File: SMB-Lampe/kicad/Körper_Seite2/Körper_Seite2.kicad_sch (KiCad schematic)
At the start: 0 parts

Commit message: Alle Platinen erstellt
Alle Platinen wurden im Projekt einzeln erstellt.
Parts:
- added C12, C13, C14, C15, C16, C17, C18, C19, C20: 100nF, Capacitor_SMD:C_0201_0603Metric, symbol Device:C
- added D12, D13, D14, D15, D16, D17, D18, D19, D20: WS2812B, LED_SMD:LED_WS2812B_PLCC4_5.0x5.0mm_P3.2mm, symbol LED:WS2812B
- added J13, J14, J15, J16, J17, J18: Conn_01x01_Pin, TestPoint:TestPoint_Pad_1.0x1.0mm, symbol Connector:Conn_01x01_Pin
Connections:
- new net: D13.4 (DIN), D14.2 (DOUT)
- new net: D14.4 (DIN), D15.2 (DOUT)
- new net: D17.4 (DIN), D18.2 (DOUT)
- new net: D18.4 (DIN), D19.2 (DOUT)
- new net: D19.4 (DIN), D20.2 (DOUT)
- new net: D15.4 (DIN), D16.2 (DOUT)
- new net: D12.4 (DIN), D13.2 (DOUT)
- new net Data: D16.4 (DIN), D17.2 (DOUT)
- new net Data_In: D12.2 (DOUT), J14.1 (Pin_1)
- new net Data_OUT: D20.4 (DIN), J17.1 (Pin_1)
- new net GND: C12.1, C12.2, C13.1, C13.2, C14.1, C14.2, C15.1, C15.2, C16.1, C16.2, C17.1, C17.2, C18.1, C18.2, C19.1, C19.2, C20.1, C20.2, D12.1 (VDD), D12.3 (VSS), D13.1 (VDD), D13.3 (VSS), D14.1 (VDD), D14.3 (VSS), D15.1 (VDD), D15.3 (VSS), D16.1 (VDD), D16.3 (VSS), D17.1 (VDD), D17.3 (VSS), D18.1 (VDD), D18.3 (VSS), D19.1 (VDD), D19.3 (VSS), D20.1 (VDD), D20.3 (VSS), J13.1 (Pin_1), J15.1 (Pin_1), J16.1 (Pin_1), J18.1 (Pin_1)

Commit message: Alle LEDs nochmal richtig angeschlossen
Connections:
- net Data: now also D16.2 (DOUT), D17.4 (DIN); no longer D16.4 (DIN), D17.2 (DOUT)
- net Data_In: now also D12.4 (DIN); no longer D12.2 (DOUT)
- net Data_OUT: now also D20.2 (DOUT); no longer D20.4 (DIN)
- net GND: no longer C12.1, C13.1, C14.1, C15.1, C16.1, C17.1, C18.1, C19.1, C20.1, D12.1 (VDD), D13.1 (VDD), D14.1 (VDD), D15.1 (VDD), D16.1 (VDD), D17.1 (VDD), D18.1 (VDD), D19.1 (VDD), D20.1 (VDD), J13.1 (Pin_1), J16.1 (Pin_1)
- net at D14.2 (DOUT): now also D15.4 (DIN); no longer D13.4 (DIN)
- net at D14.4 (DIN): now also D13.2 (DOUT); no longer D15.2 (DOUT)
- net at D18.2 (DOUT): now also D19.4 (DIN); no longer D17.4 (DIN)
- net at D18.4 (DIN): now also D17.2 (DOUT); no longer D19.2 (DOUT)
- new net: D19.2 (DOUT), D20.4 (DIN)
- new net: D15.2 (DOUT), D16.4 (DIN)
- new net: D12.2 (DOUT), D13.4 (DIN)
- new net +5V: C12.1, C13.1, C14.1, C15.1, C16.1, C17.1, C18.1, C19.1, C20.1, D12.1 (VDD), D13.1 (VDD), D14.1 (VDD), D15.1 (VDD), D16.1 (VDD), D17.1 (VDD), D18.1 (VDD), D19.1 (VDD), D20.1 (VDD), J13.1 (Pin_1), J16.1 (Pin_1)
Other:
- moved on the sheet: C12, C13, C14, C15, C16, C17, C18, C19, C20

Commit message: Hinterbein Seite 1/2 erstellt
Anschlüsse zwischen den Platinen mit MountingHoles. Eigenes MountingHole Erstellt
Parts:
- J13, J14, J15, J16, J17, J18: footprint TestPoint:TestPoint_Pad_1.0x1.0mm -> TestPoint:TestPoint_Pad_2.0x2.0mm
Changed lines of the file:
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@@
 			)
 		)
-		(property "Footprint" "TestPoint:TestPoint_Pad_1.0x1.0mm"
+		(property "Footprint" "TestPoint:TestPoint_Pad_2.0x2.0mm"
 			(at 259.08 120.65 0)
 			(effects
@@
 			)
 		)
-		(property "Footprint" "TestPoint:TestPoint_Pad_1.0x1.0mm"
+		(property "Footprint" "TestPoint:TestPoint_Pad_2.0x2.0mm"
 			(at 33.02 63.5 0)
 			(effects
@@
 			)
 		)
-		(property "Footprint" "TestPoint:TestPoint_Pad_1.0x1.0mm"
+		(property "Footprint" "TestPoint:TestPoint_Pad_2.0x2.0mm"
 			(at 33.02 25.4 0)
 			(effects
@@
 			)
 		)
-		(property "Footprint" "TestPoint:TestPoint_Pad_1.0x1.0mm"
+		(property "Footprint" "TestPoint:TestPoint_Pad_2.0x2.0mm"
 			(at 33.02 44.45 0)
 			(effects
@@
 			)
 		)
-		(property "Footprint" "TestPoint:TestPoint_Pad_1.0x1.0mm"
+		(property "Footprint" "TestPoint:TestPoint_Pad_2.0x2.0mm"
 			(at 259.08 101.6 0)
 			(effects
@@
 			)
 		)
-		(property "Footprint" "TestPoint:TestPoint_Pad_1.0x1.0mm"
+		(property "Footprint" "TestPoint:TestPoint_Pad_2.0x2.0mm"
 			(at 259.08 139.7 0)
 			(effects

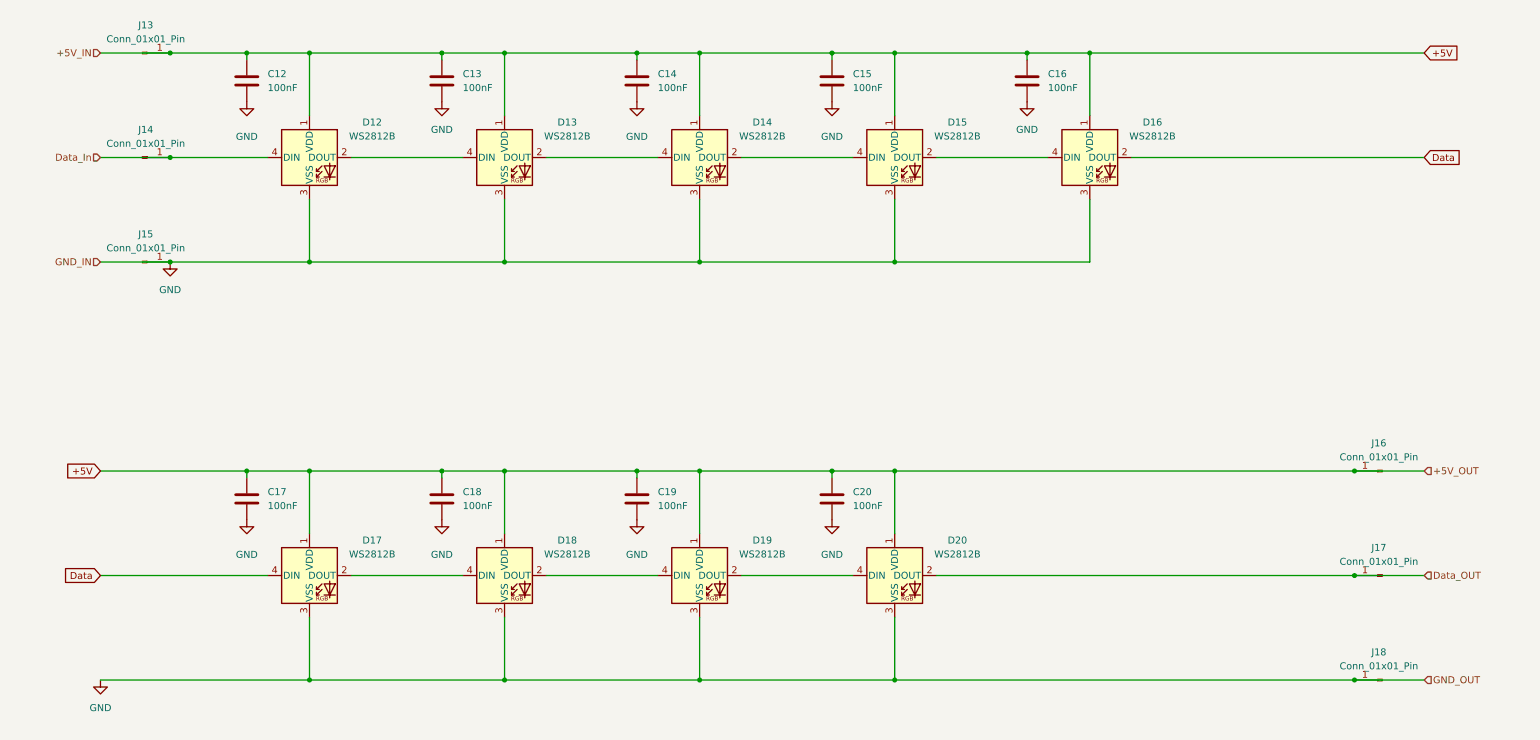
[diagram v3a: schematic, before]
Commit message: Vorderseite Platine Körper Seite 1 fertig
zwei GND Verbindungen fehlen noch
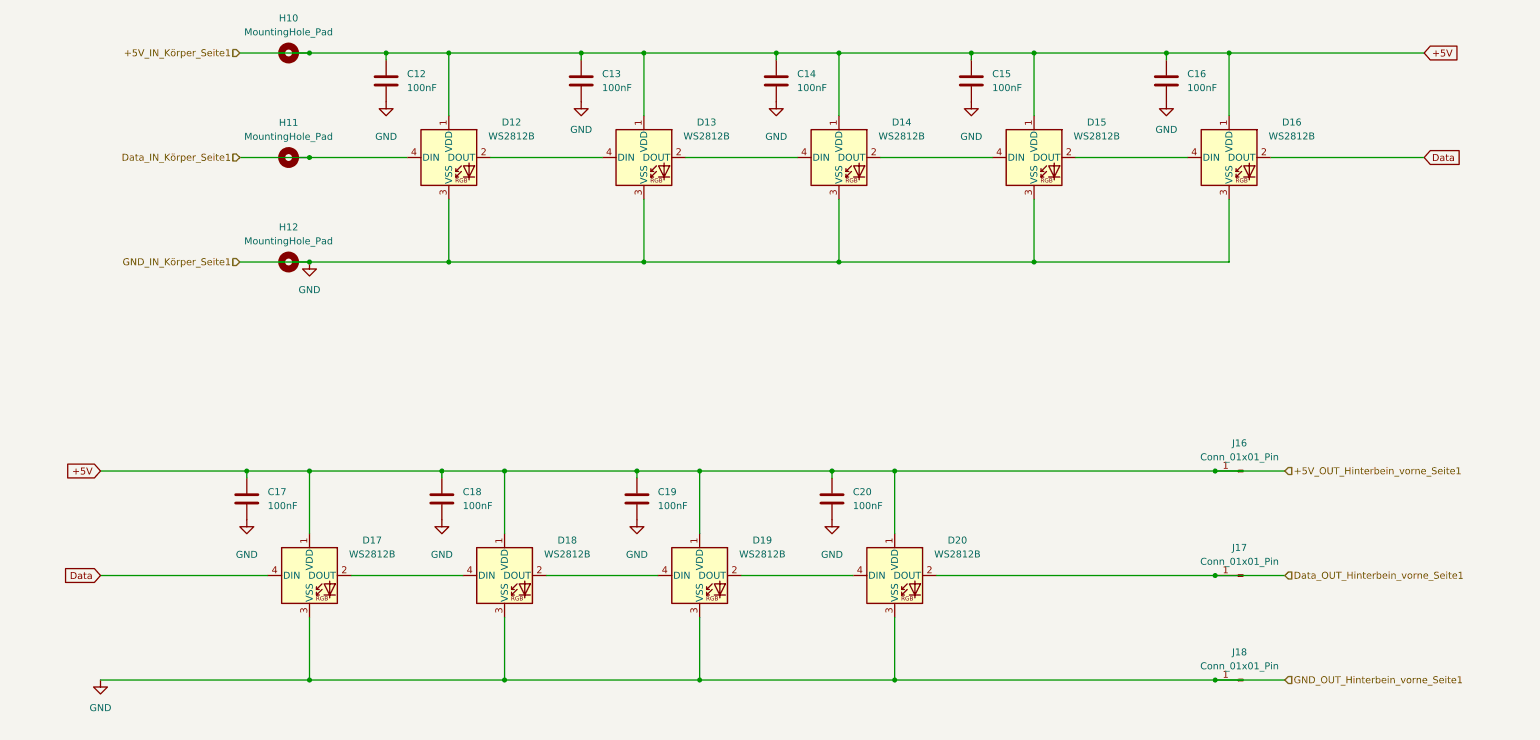
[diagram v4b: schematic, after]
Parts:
- removed J13, J14, J15: Conn_01x01_Pin, TestPoint:TestPoint_Pad_2.0x2.0mm, symbol Connector:Conn_01x01_Pin
- added H10, H11, H12: MountingHole_Pad, symbol Mechanical:MountingHole_Pad
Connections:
- net +5V: now also H10.1
- net GND: now also H12.1
- net Data_In renamed Data_IN_Körper_Seite1
- net Data_IN_Körper_Seite1: now also H11.1
- net Data_OUT renamed Data_OUT_Hinterbein_vorne_Seite1
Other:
- moved on the sheet: C12, C13, C14, C15, C16, D12, D13, D14, D15, D16, J16, J17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

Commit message: Körper mit Vorder und Rückseite fertig
Alle Leiterbahnen sind gelegt und Verbindungen zu den anderen Platinen platziert
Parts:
- added H2, H3, H6, H7: MountingHole_Pad, Eigenen_Library:MountingHole D2 x d1 test, symbol Mechanical:MountingHole_Pad
- H1: renamed from H10; footprint (none) -> Eigenen_Library:MountingHole D2 x d1 test
- H4: renamed from H11; footprint (none) -> Eigenen_Library:MountingHole D2 x d1 test
- H5: renamed from H12; footprint (none) -> Eigenen_Library:MountingHole D2 x d1 test
- renumbered C12 to C1, C13 to C2, C14 to C3, C15 to C4, C16 to C5, C17 to C6, C18 to C7, C19 to C8, C20 to C9, D12 to D1, D13 to D2, D14 to D3, D15 to D4, D16 to D5, D17 to D6, D18 to D7, D19 to D8, D20 to D9, J16 to J1, J17 to J2, J18 to J3
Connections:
- net +5V: now also H2.1, H3.1
- net GND: now also H6.1, H7.1
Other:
- note added: "+5V für LED 2-4,9 Seite 2"
- note added: "+5V für LED 5-8 Seite 2"
- note added: "GND für LED 5-8 Seite 2"
- note added: "GND für LED 5-8 Seite1"
- moved on the sheet: C1, C2, C3, C4, C5, D1, D2, D3, D4, D5, H1, H4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

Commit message: Vorderes Hinterbein fertig
Alle Platinen sind fertig beschaltet
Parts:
- renumbered C1 to C12, C2 to C13, C3 to C14, C4 to C15, C5 to C16, C6 to C17, C7 to C18, C8 to C19, C9 to C20, D1 to D12, D2 to D13, D3 to D14, D4 to D15, D5 to D16, D6 to D17, D7 to D18, D8 to D19, D9 to D20, H1 to H10, H4 to H11, H5 to H12, H2 to H14, H7 to H17, H3 to H19, H6 to H20, J1 to J16, J2 to J17, J3 to J18
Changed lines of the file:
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@@
 		(on_board yes)
 		(dnp no)
-		(property "Reference" "H6"
+		(property "Reference" "H20"
 			(at 49.276 80.01 90)
 			(effects
@@
 		(on_board yes)
 		(dnp no)
-		(property "Reference" "H4"
+		(property "Reference" "H11"
 			(at 59.944 60.706 90)
 			(effects
@@
 		(on_board yes)
 		(dnp no)
-		(property "Reference" "D3"
+		(property "Reference" "D14"
 			(at 171.45 50.7298 0)
 			(effects
@@
 		(on_board yes)
 		(dnp no)
-		(property "Reference" "H3"
+		(property "Reference" "H19"
 			(at 49.276 46.99 90)
 			(effects
@@
 		(on_board yes)
 		(dnp no)
-		(property "Reference" "#PWR0103"
+		(property "Reference" "#PWR025"
 			(at 123.19 116.84 0)
 			(effects
@@
 		(dnp no)
 		(fields_autoplaced yes)
-		(property "Reference" "#PWR0101"
+		(property "Reference" "#PWR021"
 			(at 219.71 53.34 0)
 			(effects
@@
 		(dnp no)
 		(fields_autoplaced yes)
-		(property "Reference" "C4"
+		(property "Reference" "C15"
 			(at 187.96 41.9099 0)
 			(effects
@@
 		(dnp no)
 		(fields_autoplaced yes)
-		(property "Reference" "J2"
+		(property "Reference" "J17"
 			(at 233.045 115.57 0)
 			(effects
@@
 		(dnp no)
 		(fields_autoplaced yes)
-		(property "Reference" "C2"
+		(property "Reference" "C13"
 			(at 116.84 41.9099 0)
 			(effects
@@
 		(on_board yes)
 		(dnp no)
-		(property "Reference" "D6"
+		(property "Reference" "D17"
 			(at 74.93 114.2298 0)
 			(effects
@@
 		(on_board yes)
 		(dnp no)
-		(property "Reference" "#PWR0105"
+		(property "Reference" "#PWR019"
 			(at 148.59 53.34 0)
 			(effects
@@
 		(on_board yes)
 		(dnp no)
-		(property "Reference" "D7"
+		(property "Reference" "D18"
 			(at 110.49 114.2298 0)
 			(effects
@@
 		(dnp no)
 		(fields_autoplaced yes)
-		(property "Reference" "C1"
+		(property "Reference" "C12"
 			(at 81.28 41.9099 0)
 			(effects
@@
 		(dnp no)
 		(fields_autoplaced yes)
-		(property "Reference" "#PWR0108"
+		(property "Reference" "#PWR022"
 			(at 88.9 82.55 0)
 			(effects
@@
 		(on_board yes)
 		(dnp no)
-		(property "Reference" "#PWR0104"
+		(property "Reference" "#PWR017"
 			(at 77.47 53.34 0)
 			(effects
@@
 		(on_board yes)
 		(dnp no)
-		(property "Reference" "H2"
+		(property "Reference" "H14"
 			(at 49.276 41.91 90)
 			(effects
@@
 		(on_board yes)
 		(dnp no)
-		(property "Reference" "D8"
+		(property "Reference" "D19"
 			(at 146.05 114.2298 0)
 			(effects
@@
 		(dnp no)
 		(fields_autoplaced yes)
-		(property "Reference" "C7"
+		(property "Reference" "C18"
 			(at 91.44 105.4099 0)
 			(effects
@@
 		(dnp no)
 		(fields_autoplaced yes)
-		(property "Reference" "H1"
+		(property "Reference" "H10"
 			(at 59.69 31.75 90)
 			(effects
@@
 		(dnp no)
 		(fields_autoplaced yes)
-		(property "Reference" "J1"
+		(property "Reference" "J16"
 			(at 233.045 96.52 0)
 			(effects
@@
 		(on_board yes)
 		(dnp no)
-		(property "Reference" "#PWR0111"
+		(property "Reference" "#PWR023"
 			(at 52.07 116.84 0)
 			(effects
@@
 		(on_board yes)
 		(dnp no)
-		(property "Reference" "#PWR0106"
+		(property "Reference" "#PWR020"
 			(at 184.15 53.34 0)
 			(effects
@@
 		(on_board yes)
 		(dnp no)
-		(property "Reference" "D9"
+		(property "Reference" "D20"
 			(at 181.61 114.2298 0)
 			(effects
@@
 		(on_board yes)
 		(dnp no)
-		(property "Reference" "D4"
+		(property "Reference" "D15"
 			(at 207.01 50.7298 0)
 			(effects
@@
 		(dnp no)
 		(fields_autoplaced yes)
-		(property "Reference" "C5"
+		(property "Reference" "C16"
 			(at 223.52 41.9099 0)
 			(effects
@@
 		(on_board yes)
 		(dnp no)
-		(property "Reference" "H7"
+		(property "Reference" "H17"
 			(at 234.95 143.5099 90)
 			(effects
@@
 		(on_board yes)
 		(dnp no)
-		(property "Reference" "D2"
+		(property "Reference" "D13"
 			(at 135.89 50.7298 0)
 			(effects
@@
 		(on_board yes)
 		(dnp no)
-		(property "Reference" "#PWR0110"
+		(property "Reference" "#PWR024"
 			(at 87.63 116.84 0)
 			(effects
@@
 		(on_board yes)
 		(dnp no)
-		(property "Reference" "D5"
+		(property "Reference" "D16"
 			(at 242.57 50.7298 0)
 			(effects
@@
 		(on_board yes)
 		(dnp no)
-		(property "Reference" "#PWR0107"
+		(property "Reference" "#PWR026"
 			(at 158.75 116.84 0)
 			(effects
@@
 		(dnp no)
 		(fields_autoplaced yes)
-		(property "Reference" "#PWR0102"
+		(property "Reference" "#PWR018"
 			(at 113.03 53.34 0)
 			(effects
@@
 		(dnp no)
 		(fields_autoplaced yes)
-		(property "Reference" "C6"
+		(property "Reference" "C17"
 			(at 55.88 105.4099 0)
 			(effects
@@
 		(dnp no)
 		(fields_autoplaced yes)
-		(property "Reference" "C8"
+		(property "Reference" "C19"
 			(at 127 105.4099 0)
 			(effects
@@
 		(dnp no)
 		(fields_autoplaced yes)
-		(property "Reference" "#PWR0109"
+		(property "Reference" "#PWR027"
 			(at 25.4 146.05 0)
 			(effects
@@
 		(dnp no)
 		(fields_autoplaced yes)
-		(property "Reference" "J3"
+		(property "Reference" "J18"
 			(at 233.045 134.62 0)
 			(effects
@@
 		(dnp no)
 		(fields_autoplaced yes)
-		(property "Reference" "C9"
+		(property "Reference" "C20"
 			(at 162.56 105.4099 0)
 			(effects
@@
 		(dnp no)
 		(fields_autoplaced yes)
-		(property "Reference" "C3"
+		(property "Reference" "C14"
 			(at 152.4 41.9099 0)
 			(effects
@@
 		(on_board yes)
 		(dnp no)
-		(property "Reference" "D1"
+		(property "Reference" "D12"
 			(at 100.33 50.7298 0)
 			(effects
@@
 		(dnp no)
 		(fields_autoplaced yes)
-		(property "Reference" "H5"
+		(property "Reference" "H12"
 			(at 59.69 69.85 90)
 			(effects

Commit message: Hinterbeine Geändert teilweiße Körper
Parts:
- C12, C13, C14, C15, C16, C17, C18, C19, C20: footprint Capacitor_SMD:C_0201_0603Metric -> Capacitor_SMD:C_0603_1608Metric_Pad1.08x0.95mm_HandSolder
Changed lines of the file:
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@@
 			)
 		)
-		(property "Footprint" "Capacitor_SMD:C_0201_0603Metric"
+		(property "Footprint" "Capacitor_SMD:C_0603_1608Metric_Pad1.08x0.95mm_HandSolder"
 			(at 185.1152 46.99 0)
 			(effects
@@
 			)
 		)
-		(property "Footprint" "Capacitor_SMD:C_0201_0603Metric"
+		(property "Footprint" "Capacitor_SMD:C_0603_1608Metric_Pad1.08x0.95mm_HandSolder"
 			(at 113.9952 46.99 0)
 			(effects
@@
 			)
 		)
-		(property "Footprint" "Capacitor_SMD:C_0201_0603Metric"
+		(property "Footprint" "Capacitor_SMD:C_0603_1608Metric_Pad1.08x0.95mm_HandSolder"
 			(at 78.4352 46.99 0)
 			(effects
@@
 			)
 		)
-		(property "Footprint" "Capacitor_SMD:C_0201_0603Metric"
+		(property "Footprint" "Capacitor_SMD:C_0603_1608Metric_Pad1.08x0.95mm_HandSolder"
 			(at 88.5952 110.49 0)
 			(effects
@@
 			)
 		)
-		(property "Footprint" "Capacitor_SMD:C_0201_0603Metric"
+		(property "Footprint" "Capacitor_SMD:C_0603_1608Metric_Pad1.08x0.95mm_HandSolder"
 			(at 220.6752 46.99 0)
 			(effects
@@
 			)
 		)
-		(property "Footprint" "Capacitor_SMD:C_0201_0603Metric"
+		(property "Footprint" "Capacitor_SMD:C_0603_1608Metric_Pad1.08x0.95mm_HandSolder"
 			(at 53.0352 110.49 0)
 			(effects
@@
 			)
 		)
-		(property "Footprint" "Capacitor_SMD:C_0201_0603Metric"
+		(property "Footprint" "Capacitor_SMD:C_0603_1608Metric_Pad1.08x0.95mm_HandSolder"
 			(at 124.1552 110.49 0)
 			(effects
@@
 			)
 		)
-		(property "Footprint" "Capacitor_SMD:C_0201_0603Metric"
+		(property "Footprint" "Capacitor_SMD:C_0603_1608Metric_Pad1.08x0.95mm_HandSolder"
 			(at 159.7152 110.49 0)
 			(effects
@@
 			)
 		)
-		(property "Footprint" "Capacitor_SMD:C_0201_0603Metric"
+		(property "Footprint" "Capacitor_SMD:C_0603_1608Metric_Pad1.08x0.95mm_HandSolder"
 			(at 149.5552 46.99 0)
 			(effects
